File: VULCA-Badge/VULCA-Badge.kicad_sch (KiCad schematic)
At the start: 9 parts, among them SW1 SW_SPST

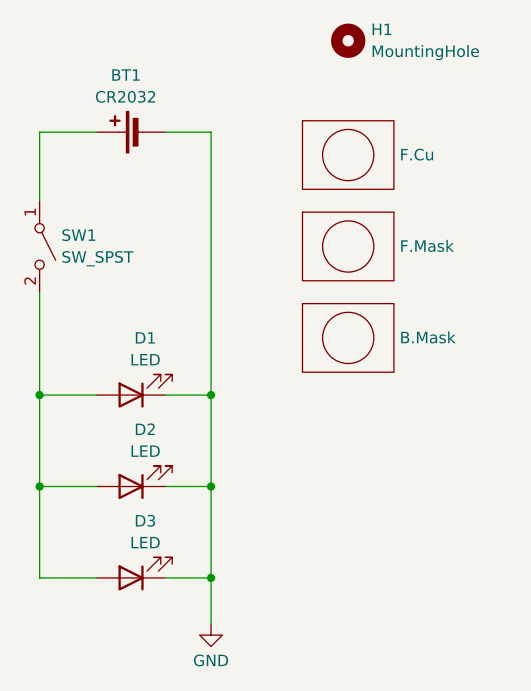
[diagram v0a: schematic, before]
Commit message: Aligns all LEDs with the same orientation
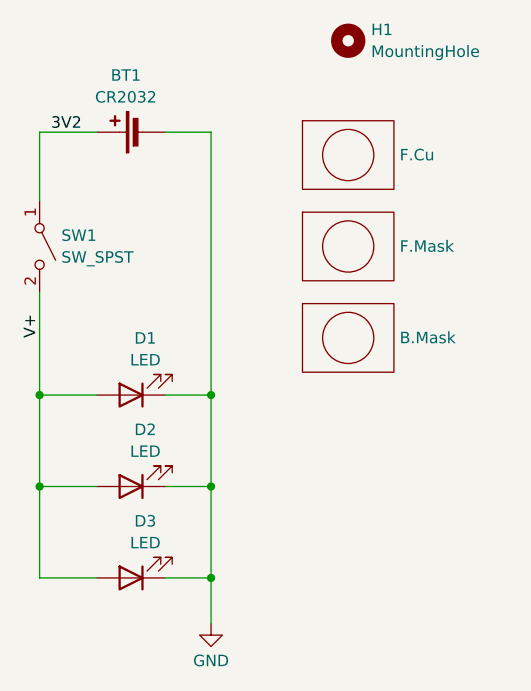
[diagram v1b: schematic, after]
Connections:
- net V+: now reaches D1.2 (A), D2.2 (A), D3.2 (A), SW1.2 (B)
- net 3V2: now reaches BT1.1 (+), SW1.1 (A)
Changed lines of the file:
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@@
+		)
+	)
+	(label "V+"
+		(at 125.73 67.31 90)
+		(effects
+			(font
+				(size 1.27 1.27)
+			)
+			(justify left bottom)
+		)
+	)
+	(label "3V2"
+		(at 127 44.45 0)
+		(effects
+			(font
+				(size 1.27 1.27)
+			)
+			(justify left bottom)
 		)
 	)

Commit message: ZAM coloured badges
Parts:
- Lg1, Lg2, Lg3: now left out of the parts list
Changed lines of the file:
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@@
 		(unit 1)
 		(exclude_from_sim no)
-		(in_bom yes)
+		(in_bom no)
 		(on_board yes)
 		(dnp no)
@@
 			)
 		)
+		(property "Purpose" ""
+			(at 160.02 57.15 0)
+			(effects
+				(font
+					(size 1.27 1.27)
+				)
+			)
+		)
 		(instances
 			(project ""
@@
 		(unit 1)
 		(exclude_from_sim no)
-		(in_bom yes)
+		(in_bom no)
 		(on_board yes)
 		(dnp no)
@@
 		(at 160.02 34.29 0)
 		(unit 1)
-		(exclude_from_sim yes)
+		(exclude_from_sim no)
 		(in_bom no)
 		(on_board yes)
@@
 			)
 		)
+		(property "Purpose" ""
+			(at 160.02 34.29 0)
+			(effects
+				(font
+					(size 1.27 1.27)
+				)
+				(hide yes)
+			)
+		)
 		(instances
 			(project ""
@@
 		(unit 1)
 		(exclude_from_sim no)
-		(in_bom yes)
+		(in_bom no)
 		(on_board yes)
 		(dnp no)
@@
 			)
 		)
+		(property "Purpose" ""
+			(at 160.02 46.99 0)
+			(effects
+				(font
+					(size 1.27 1.27)
+				)
+			)
+		)
